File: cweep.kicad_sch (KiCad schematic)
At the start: 59 parts

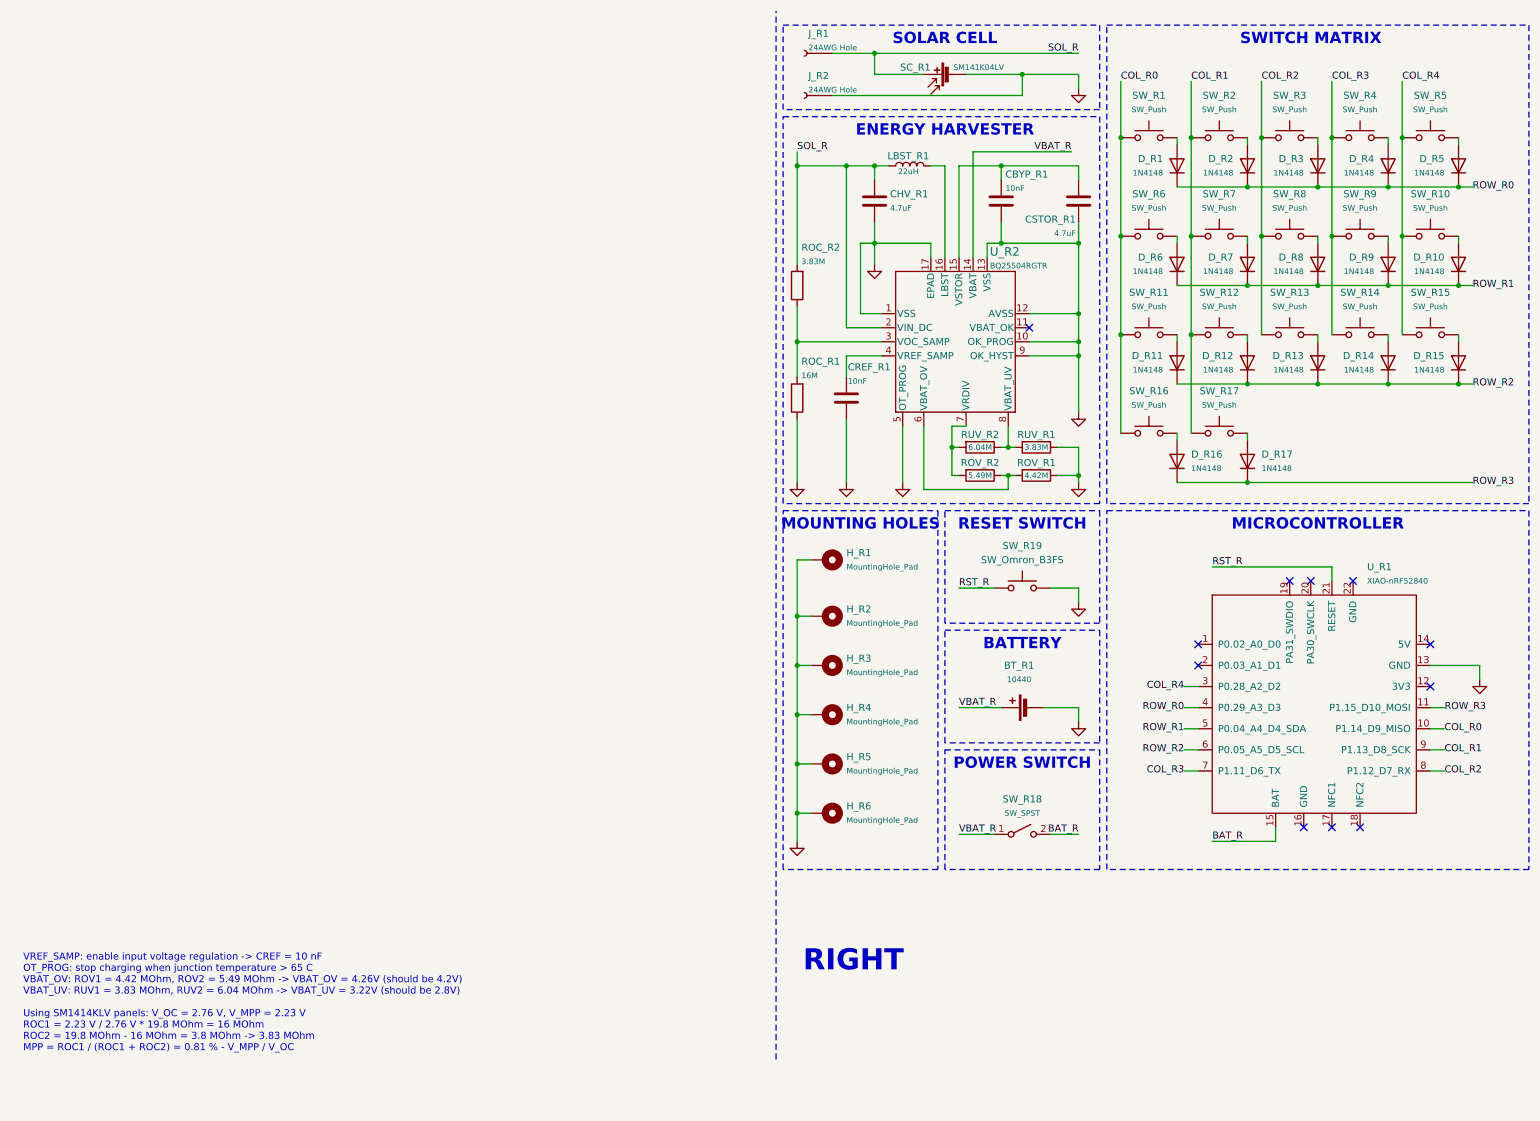
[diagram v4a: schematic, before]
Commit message: feat: add left side of schematic
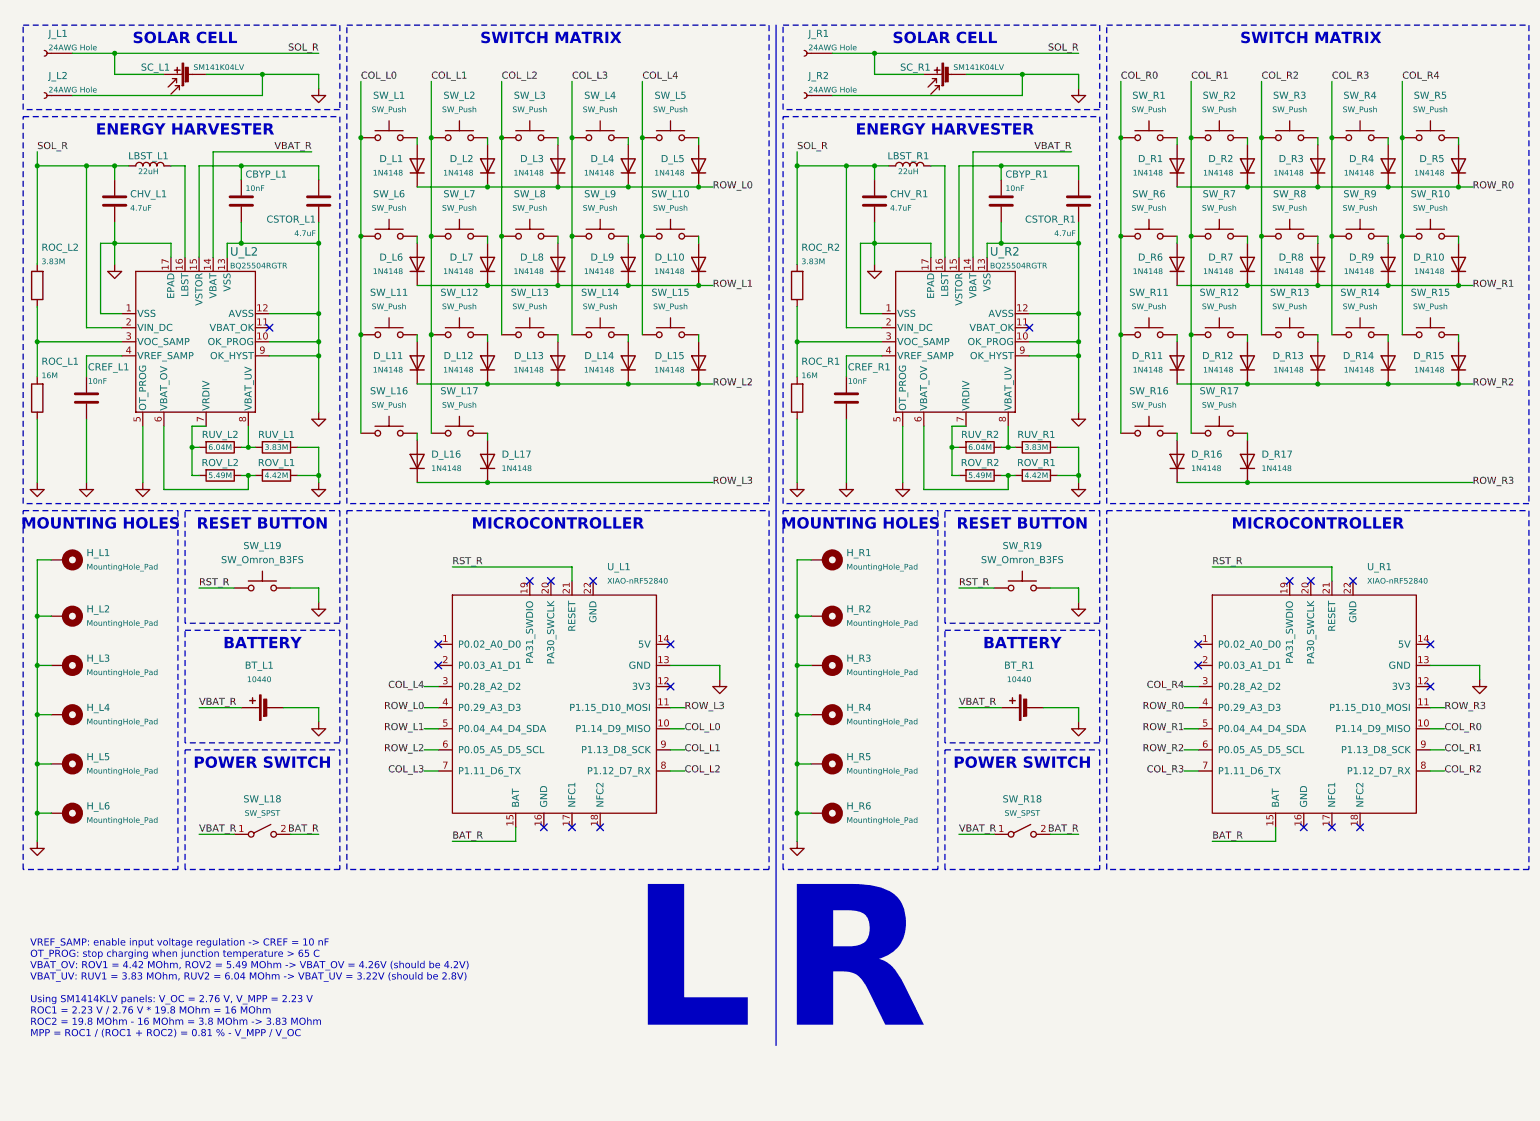
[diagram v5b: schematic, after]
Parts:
- added BT_L1: 10440, com_snapeda_Keystone:BatteryHolder_Keystone_230-1_1x10440, symbol Device:Battery_Cell
- added CBYP_R1, CREF_R1: 10nF, Capacitor_SMD:C_0603_1608Metric_Pad1.08x0.95mm_HandSolder, symbol Device:C
- added CHV_R1, CSTOR_R1: 4.7uF, Capacitor_SMD:C_0603_1608Metric_Pad1.08x0.95mm_HandSolder, symbol Device:C
- added D_R1, D_R10, D_R11, D_R12, D_R13, D_R14, D_R15, D_R16, D_R17, D_R2, D_R3, D_R4, D_R5, D_R6, D_R7, D_R8, D_R9: 1N4148, Diode_THT:D_DO-35_SOD27_P7.62mm_Horizontal, symbol Diode:1N4148
- added H_L1, H_L2, H_L3, H_L4, H_L5, H_L6: MountingHole_Pad, MountingHole:MountingHole_2.2mm_M2_DIN965_Pad_TopOnly, symbol Mechanical:MountingHole_Pad
- added J_R1, J_R2: 24AWG Hole, Connector_Wire:SolderWire-0.127sqmm_1x01_D0.48mm_OD1mm_Relief, symbol Connector:Conn_01x01_Socket
- added LBST_R1: 22uH, Inductor_SMD:L_1210_3225Metric_Pad1.42x2.65mm_HandSolder, symbol Device:L
- added ROC_R1: 16M, Resistor_SMD:R_0603_1608Metric_Pad0.98x0.95mm_HandSolder, symbol Device:R
- added ROC_R2, RUV_R1: 3.83M, Resistor_SMD:R_0603_1608Metric_Pad0.98x0.95mm_HandSolder, symbol Device:R
- added ROV_R1: 4.42M, Resistor_SMD:R_0603_1608Metric_Pad0.98x0.95mm_HandSolder, symbol Device:R
- added ROV_R2: 5.49M, Resistor_SMD:R_0603_1608Metric_Pad0.98x0.95mm_HandSolder, symbol Device:R
- added RUV_R2: 6.04M, Resistor_SMD:R_0603_1608Metric_Pad0.98x0.95mm_HandSolder, symbol Device:R
- added SC_R1: SM141K04LV, cweep:SM141K04LV, symbol Device:Solar_Cell
- added SW_L18: SW_SPST, KAN-15:SW_KAN-15_PHT, symbol Switch:SW_SPST
- added SW_L19: SW_Omron_B3FS, Button_Switch_THT:SW_TH_Tactile_Omron_B3F-10xx, symbol Switch:SW_Omron_B3FS
- added SW_R1, SW_R10, SW_R11, SW_R12, SW_R13, SW_R14, SW_R15, SW_R16, SW_R17, SW_R2, SW_R3, SW_R4, SW_R5, SW_R6, SW_R7, SW_R8, SW_R9: SW_Push, Switch_Keyboard_Hotswap_Kailh:SW_Hotswap_Kailh_Choc_V1_1.00u, symbol Switch:SW_Push
- added U_L1: XIAO-nRF52840, Seeed Studio XIAO Series Library:XIAO-nRF52840, symbol Seeed Studio XIAO Series:XIAO-nRF52840
- added U_R2: BQ25504RGTR, BQ25504RGTR:RGT16_1P7X1P7, symbol BQ25504RGTR:BQ25504RGTR
- renumbered CBYP_R1 to CBYP_L1, CHV_R1 to CHV_L1, CREF_R1 to CREF_L1, CSTOR_R1 to CSTOR_L1, D_R1 to D_L1, D_R10 to D_L10, D_R11 to D_L11, D_R12 to D_L12, D_R13 to D_L13, D_R14 to D_L14, D_R15 to D_L15, D_R16 to D_L16, D_R17 to D_L17, D_R2 to D_L2, D_R3 to D_L3, D_R4 to D_L4, D_R5 to D_L5, D_R6 to D_L6, D_R7 to D_L7, D_R8 to D_L8, D_R9 to D_L9, J_R1 to J_L1, J_R2 to J_L2, LBST_R1 to LBST_L1, ROC_R1 to ROC_L1, ROC_R2 to ROC_L2, ROV_R1 to ROV_L1, ROV_R2 to ROV_L2, RUV_R1 to RUV_L1, RUV_R2 to RUV_L2, SC_R1 to SC_L1, SW_R1 to SW_L1, SW_R10 to SW_L10, SW_R11 to SW_L11, SW_R12 to SW_L12, SW_R13 to SW_L13, SW_R14 to SW_L14, SW_R15 to SW_L15, SW_R16 to SW_L16, SW_R17 to SW_L17, SW_R2 to SW_L2, SW_R3 to SW_L3, SW_R4 to SW_L4, SW_R5 to SW_L5, SW_R6 to SW_L6, SW_R7 to SW_L7, SW_R8 to SW_L8, SW_R9 to SW_L9, U_R2 to U_L2
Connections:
- net BAT_R: now also SW_L18.2 (B), U_L1.15 (BAT)
- net COL_R0: now also SW_R1.1, SW_R11.1, SW_R16.1, SW_R6.1; no longer SW_L1.1, SW_L11.1, SW_L16.1, SW_L6.1
- net COL_R1: now also SW_R12.1, SW_R17.1, SW_R2.1, SW_R7.1; no longer SW_L12.1, SW_L17.1, SW_L2.1, SW_L7.1
- net COL_R2: now also SW_R13.1, SW_R3.1, SW_R8.1; no longer SW_L13.1, SW_L3.1, SW_L8.1
- net COL_R3: now also SW_R14.1, SW_R4.1, SW_R9.1; no longer SW_L14.1, SW_L4.1, SW_L9.1
- net COL_R4: now also SW_R10.1, SW_R15.1, SW_R5.1; no longer SW_L10.1, SW_L15.1, SW_L5.1
- net GND: now also BT_L1.2 (-), CBYP_R1.2, CHV_R1.2, CREF_R1.2, CSTOR_R1.2, H_L1.1, H_L2.1, H_L3.1, H_L4.1, H_L5.1, H_L6.1, J_R2.1 (Pin_1), ROC_R1.1, ROV_R1.1, RUV_R1.1, SC_R1.2 (-), SW_L19.2, U_L1.13 (GND), U_R2.1 (VSS), U_R2.10 (OK_PROG), U_R2.12 (AVSS), U_R2.13 (VSS), U_R2.17 (EPAD), U_R2.5 (OT_PROG), U_R2.9 (OK_HYST)
- net ROW_R0: now also D_R1.1 (K), D_R2.1 (K), D_R3.1 (K), D_R4.1 (K), D_R5.1 (K); no longer D_L1.1 (K), D_L2.1 (K), D_L3.1 (K), D_L4.1 (K), D_L5.1 (K)
- net ROW_R1: now also D_R10.1 (K), D_R6.1 (K), D_R7.1 (K), D_R8.1 (K), D_R9.1 (K); no longer D_L10.1 (K), D_L6.1 (K), D_L7.1 (K), D_L8.1 (K), D_L9.1 (K)
- net ROW_R2: now also D_R11.1 (K), D_R12.1 (K), D_R13.1 (K), D_R14.1 (K), D_R15.1 (K); no longer D_L11.1 (K), D_L12.1 (K), D_L13.1 (K), D_L14.1 (K), D_L15.1 (K)
- net ROW_R3: now also D_R16.1 (K), D_R17.1 (K); no longer D_L16.1 (K), D_L17.1 (K)
- net RST_R: now also SW_L19.1, U_L1.21 (RESET)
- net SOL_R: now also CHV_R1.1, J_R1.1 (Pin_1), LBST_R1.1, ROC_R2.2, SC_R1.1 (+), U_R2.2 (VIN_DC)
- net VBAT_R: now also BT_L1.1 (+), SW_L18.1 (A), U_R2.14 (VBAT)
- new net: D_R3.2 (A), SW_R3.2
- new net: D_R5.2 (A), SW_R5.2
- new net: D_R4.2 (A), SW_R4.2
- new net: D_R2.2 (A), SW_R2.2
- new net: D_R13.2 (A), SW_R13.2
- new net: D_R15.2 (A), SW_R15.2
- new net: ROC_R1.2, ROC_R2.1, U_R2.3 (VOC_SAMP)
- new net: D_R12.2 (A), SW_R12.2
- new net: D_R10.2 (A), SW_R10.2
- new net: D_R8.2 (A), SW_R8.2
- new net: RUV_R1.2, RUV_R2.1, U_R2.8 (VBAT_UV)
- new net: D_R9.2 (A), SW_R9.2
- new net: D_R11.2 (A), SW_R11.2
- new net: ROV_R1.2, ROV_R2.1, U_R2.6 (VBAT_OV)
- new net: D_R6.2 (A), SW_R6.2
- new net: D_R17.2 (A), SW_R17.2
- new net: D_R14.2 (A), SW_R14.2
- new net: CBYP_R1.1, CSTOR_R1.1, U_R2.15 (VSTOR)
- new net: ROV_R2.2, RUV_R2.2, U_R2.7 (VRDIV)
- new net: LBST_R1.2, U_R2.16 (LBST)
- new net: D_R7.2 (A), SW_R7.2
- new net: CREF_R1.1, U_R2.4 (VREF_SAMP)
- new net: D_R16.2 (A), SW_R16.2
- new net: D_R1.2 (A), SW_R1.2
- new net COL_L0: SW_L1.1, SW_L11.1, SW_L16.1, SW_L6.1, U_L1.10 (P1.14_D9_MISO)
- new net COL_L1: SW_L12.1, SW_L17.1, SW_L2.1, SW_L7.1, U_L1.9 (P1.13_D8_SCK)
- new net COL_L2: SW_L13.1, SW_L3.1, SW_L8.1, U_L1.8 (P1.12_D7_RX)
- new net COL_L3: SW_L14.1, SW_L4.1, SW_L9.1, U_L1.7 (P1.11_D6_TX)
- new net COL_L4: SW_L10.1, SW_L15.1, SW_L5.1, U_L1.3 (P0.28_A2_D2)
- new net ROW_L0: D_L1.1 (K), D_L2.1 (K), D_L3.1 (K), D_L4.1 (K), D_L5.1 (K), U_L1.4 (P0.29_A3_D3)
- new net ROW_L1: D_L10.1 (K), D_L6.1 (K), D_L7.1 (K), D_L8.1 (K), D_L9.1 (K), U_L1.5 (P0.04_A4_D4_SDA)
- new net ROW_L2: D_L11.1 (K), D_L12.1 (K), D_L13.1 (K), D_L14.1 (K), D_L15.1 (K), U_L1.6 (P0.05_A5_D5_SCL)
- new net ROW_L3: D_L16.1 (K), D_L17.1 (K), U_L1.11 (P1.15_D10_MOSI)
- no-connect marks 11 -> 22
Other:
- note added: "L"
- note added: "R"
- note added: "RESET BUTTON"
- note removed: "RESET SWITCH"
- note removed: "RIGHT"
- moved on the sheet: CBYP_L1, CHV_L1, CREF_L1, CSTOR_L1, D_L1, D_L10, D_L11, D_L12, D_L13, D_L14, D_L15, D_L16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

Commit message: feat: make keyboard switch reversible
* fix: use SMD diode to accommodate reversible switch
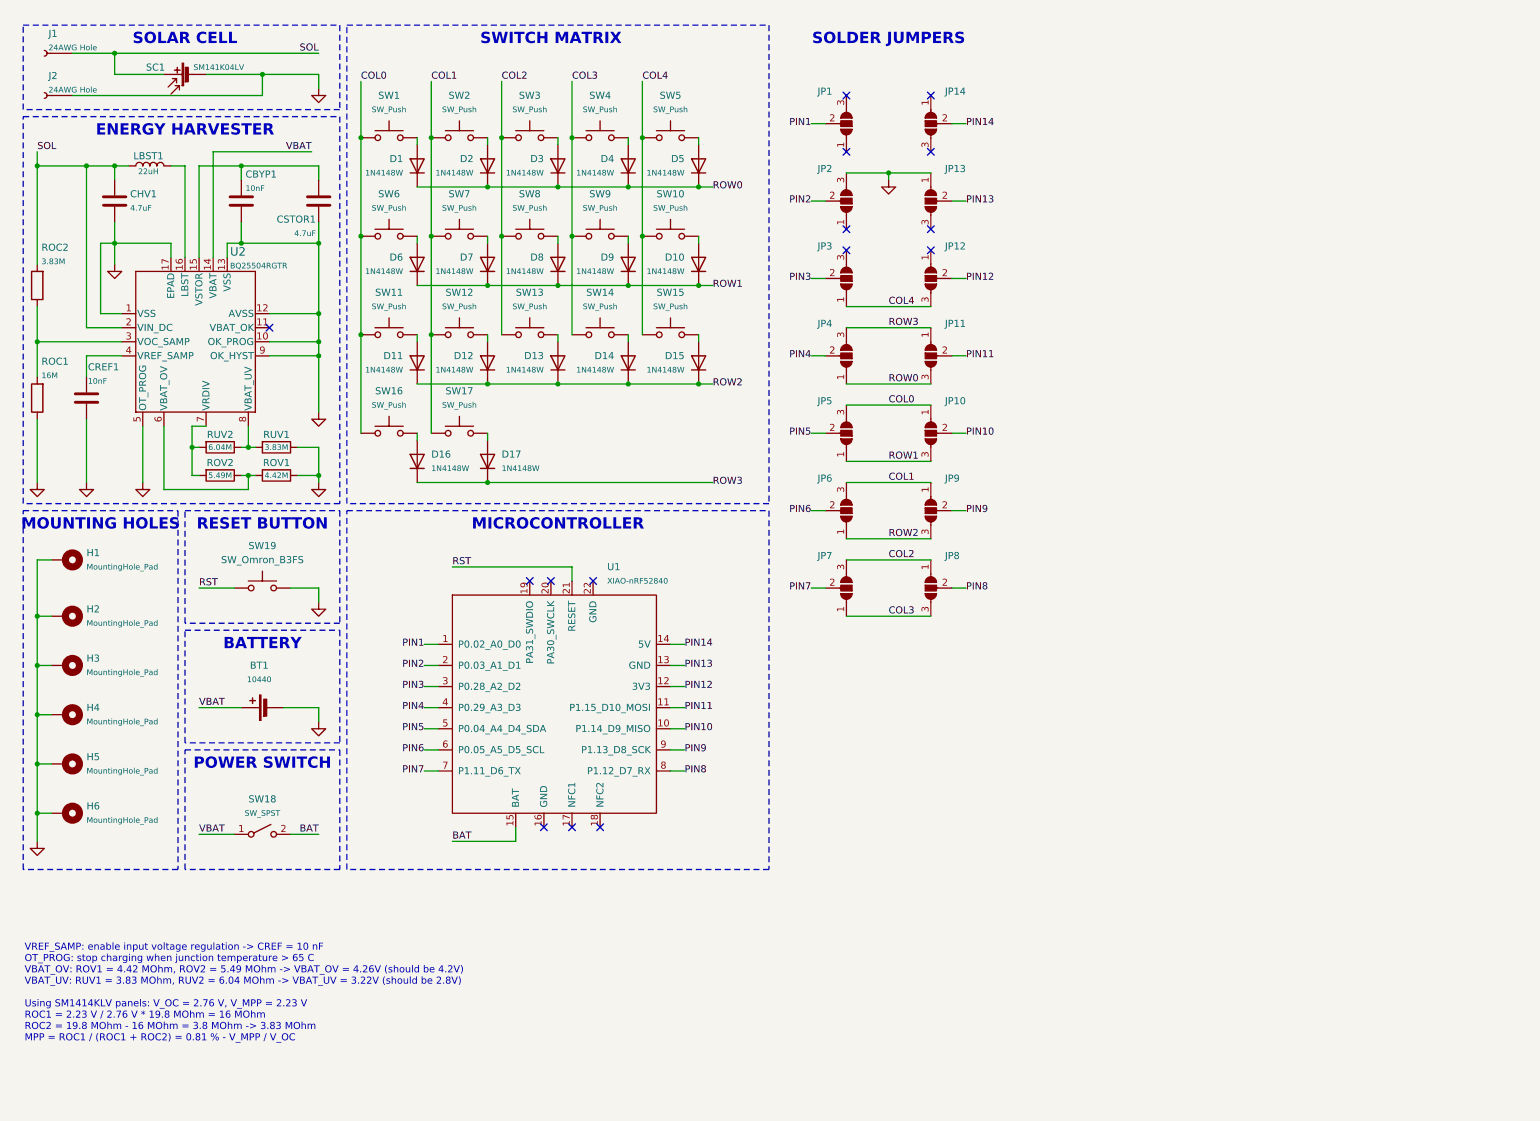
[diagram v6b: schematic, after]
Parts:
- removed BT_L1: 10440, com_snapeda_Keystone:BatteryHolder_Keystone_230-1_1x10440, symbol Device:Battery_Cell
- removed CBYP_L1, CREF_L1: 10nF, Capacitor_SMD:C_0603_1608Metric_Pad1.08x0.95mm_HandSolder, symbol Device:C
- removed CHV_L1, CSTOR_L1: 4.7uF, Capacitor_SMD:C_0603_1608Metric_Pad1.08x0.95mm_HandSolder, symbol Device:C
- removed D_L1, D_L10, D_L11, D_L12, D_L13, D_L14, D_L15, D_L16, D_L17, D_L2, D_L3, D_L4, D_L5, D_L6, D_L7, D_L8, D_L9: 1N4148, Diode_THT:D_DO-35_SOD27_P7.62mm_Horizontal, symbol Diode:1N4148
- removed H_L1, H_L2, H_L3, H_L4, H_L5, H_L6: MountingHole_Pad, MountingHole:MountingHole_2.2mm_M2_DIN965_Pad_TopOnly, symbol Mechanical:MountingHole_Pad
- removed J_L1, J_L2: 24AWG Hole, Connector_Wire:SolderWire-0.127sqmm_1x01_D0.48mm_OD1mm_Relief, symbol Connector:Conn_01x01_Socket
- removed LBST_L1: 22uH, Inductor_SMD:L_1210_3225Metric_Pad1.42x2.65mm_HandSolder, symbol Device:L
- removed ROC_L1: 16M, Resistor_SMD:R_0603_1608Metric_Pad0.98x0.95mm_HandSolder, symbol Device:R
- removed ROC_L2, RUV_L1: 3.83M, Resistor_SMD:R_0603_1608Metric_Pad0.98x0.95mm_HandSolder, symbol Device:R
- removed ROV_L1: 4.42M, Resistor_SMD:R_0603_1608Metric_Pad0.98x0.95mm_HandSolder, symbol Device:R
- removed ROV_L2: 5.49M, Resistor_SMD:R_0603_1608Metric_Pad0.98x0.95mm_HandSolder, symbol Device:R
- removed RUV_L2: 6.04M, Resistor_SMD:R_0603_1608Metric_Pad0.98x0.95mm_HandSolder, symbol Device:R
- removed SC_L1: SM141K04LV, cweep:SM141K04LV, symbol Device:Solar_Cell
- removed SW_L1, SW_L10, SW_L11, SW_L12, SW_L13, SW_L14, SW_L15, SW_L16, SW_L17, SW_L2, SW_L3, SW_L4, SW_L5, SW_L6, SW_L7, SW_L8, SW_L9: SW_Push, Switch_Keyboard_Hotswap_Kailh:SW_Hotswap_Kailh_Choc_V1_1.00u, symbol Switch:SW_Push
- removed SW_L18: SW_SPST, KAN-15:SW_KAN-15_PHT, symbol Switch:SW_SPST
- removed SW_L19: SW_Omron_B3FS, Button_Switch_THT:SW_TH_Tactile_Omron_B3F-10xx, symbol Switch:SW_Omron_B3FS
- removed U_L1: XIAO-nRF52840, Seeed Studio XIAO Series Library:XIAO-nRF52840, symbol Seeed Studio XIAO Series:XIAO-nRF52840
- removed U_L2: BQ25504RGTR, BQ25504RGTR:RGT16_1P7X1P7, symbol BQ25504RGTR:BQ25504RGTR
- added JP1, JP10, JP11, JP12, JP13, JP14, JP2, JP3, JP4, JP5, JP6, JP7, JP8, JP9: SolderJumper_3_Open, cweep:SolderJumper-3_P2.0mm_Open_TrianglePad1.0x1.5mm_Reversible, symbol Jumper:SolderJumper_3_Open
- D1: renamed from D_R1; value 1N4148 -> 1N4148W; footprint Diode_THT:D_DO-35_SOD27_P7.62mm_Horizontal -> cweep:D_SOD-123_Reversible; symbol Diode:1N4148 -> Diode:1N4148W
- D10: renamed from D_R10; value 1N4148 -> 1N4148W; footprint Diode_THT:D_DO-35_SOD27_P7.62mm_Horizontal -> cweep:D_SOD-123_Reversible; symbol Diode:1N4148 -> Diode:1N4148W
- D11: renamed from D_R11; value 1N4148 -> 1N4148W; footprint Diode_THT:D_DO-35_SOD27_P7.62mm_Horizontal -> cweep:D_SOD-123_Reversible; symbol Diode:1N4148 -> Diode:1N4148W
- D12: renamed from D_R12; value 1N4148 -> 1N4148W; footprint Diode_THT:D_DO-35_SOD27_P7.62mm_Horizontal -> cweep:D_SOD-123_Reversible; symbol Diode:1N4148 -> Diode:1N4148W
- D13: renamed from D_R13; value 1N4148 -> 1N4148W; footprint Diode_THT:D_DO-35_SOD27_P7.62mm_Horizontal -> cweep:D_SOD-123_Reversible; symbol Diode:1N4148 -> Diode:1N4148W
- D14: renamed from D_R14; value 1N4148 -> 1N4148W; footprint Diode_THT:D_DO-35_SOD27_P7.62mm_Horizontal -> cweep:D_SOD-123_Reversible; symbol Diode:1N4148 -> Diode:1N4148W
- D15: renamed from D_R15; value 1N4148 -> 1N4148W; footprint Diode_THT:D_DO-35_SOD27_P7.62mm_Horizontal -> cweep:D_SOD-123_Reversible; symbol Diode:1N4148 -> Diode:1N4148W
- D16: renamed from D_R16; value 1N4148 -> 1N4148W; footprint Diode_THT:D_DO-35_SOD27_P7.62mm_Horizontal -> cweep:D_SOD-123_Reversible; symbol Diode:1N4148 -> Diode:1N4148W
- D17: renamed from D_R17; value 1N4148 -> 1N4148W; footprint Diode_THT:D_DO-35_SOD27_P7.62mm_Horizontal -> cweep:D_SOD-123_Reversible; symbol Diode:1N4148 -> Diode:1N4148W
- D2: renamed from D_R2; value 1N4148 -> 1N4148W; footprint Diode_THT:D_DO-35_SOD27_P7.62mm_Horizontal -> cweep:D_SOD-123_Reversible; symbol Diode:1N4148 -> Diode:1N4148W
- D3: renamed from D_R3; value 1N4148 -> 1N4148W; footprint Diode_THT:D_DO-35_SOD27_P7.62mm_Horizontal -> cweep:D_SOD-123_Reversible; symbol Diode:1N4148 -> Diode:1N4148W
- D4: renamed from D_R4; value 1N4148 -> 1N4148W; footprint Diode_THT:D_DO-35_SOD27_P7.62mm_Horizontal -> cweep:D_SOD-123_Reversible; symbol Diode:1N4148 -> Diode:1N4148W
- D5: renamed from D_R5; value 1N4148 -> 1N4148W; footprint Diode_THT:D_DO-35_SOD27_P7.62mm_Horizontal -> cweep:D_SOD-123_Reversible; symbol Diode:1N4148 -> Diode:1N4148W
- D6: renamed from D_R6; value 1N4148 -> 1N4148W; footprint Diode_THT:D_DO-35_SOD27_P7.62mm_Horizontal -> cweep:D_SOD-123_Reversible; symbol Diode:1N4148 -> Diode:1N4148W
- D7: renamed from D_R7; value 1N4148 -> 1N4148W; footprint Diode_THT:D_DO-35_SOD27_P7.62mm_Horizontal -> cweep:D_SOD-123_Reversible; symbol Diode:1N4148 -> Diode:1N4148W
- D8: renamed from D_R8; value 1N4148 -> 1N4148W; footprint Diode_THT:D_DO-35_SOD27_P7.62mm_Horizontal -> cweep:D_SOD-123_Reversible; symbol Diode:1N4148 -> Diode:1N4148W
- D9: renamed from D_R9; value 1N4148 -> 1N4148W; footprint Diode_THT:D_DO-35_SOD27_P7.62mm_Horizontal -> cweep:D_SOD-123_Reversible; symbol Diode:1N4148 -> Diode:1N4148W
- SW1: renamed from SW_R1; footprint Switch_Keyboard_Hotswap_Kailh:SW_Hotswap_Kailh_Choc_V1_1.00u -> cweep:SW_Hotswap_Kailh_Choc_V1_1.00u_Reversible
- SW10: renamed from SW_R10; footprint Switch_Keyboard_Hotswap_Kailh:SW_Hotswap_Kailh_Choc_V1_1.00u -> cweep:SW_Hotswap_Kailh_Choc_V1_1.00u_Reversible
- SW11: renamed from SW_R11; footprint Switch_Keyboard_Hotswap_Kailh:SW_Hotswap_Kailh_Choc_V1_1.00u -> cweep:SW_Hotswap_Kailh_Choc_V1_1.00u_Reversible
- SW12: renamed from SW_R12; footprint Switch_Keyboard_Hotswap_Kailh:SW_Hotswap_Kailh_Choc_V1_1.00u -> cweep:SW_Hotswap_Kailh_Choc_V1_1.00u_Reversible
- SW13: renamed from SW_R13; footprint Switch_Keyboard_Hotswap_Kailh:SW_Hotswap_Kailh_Choc_V1_1.00u -> cweep:SW_Hotswap_Kailh_Choc_V1_1.00u_Reversible
- SW14: renamed from SW_R14; footprint Switch_Keyboard_Hotswap_Kailh:SW_Hotswap_Kailh_Choc_V1_1.00u -> cweep:SW_Hotswap_Kailh_Choc_V1_1.00u_Reversible
- SW15: renamed from SW_R15; footprint Switch_Keyboard_Hotswap_Kailh:SW_Hotswap_Kailh_Choc_V1_1.00u -> cweep:SW_Hotswap_Kailh_Choc_V1_1.00u_Reversible
- SW16: renamed from SW_R16; footprint Switch_Keyboard_Hotswap_Kailh:SW_Hotswap_Kailh_Choc_V1_1.00u -> cweep:SW_Hotswap_Kailh_Choc_V1_1.00u_Reversible
- SW17: renamed from SW_R17; footprint Switch_Keyboard_Hotswap_Kailh:SW_Hotswap_Kailh_Choc_V1_1.00u -> cweep:SW_Hotswap_Kailh_Choc_V1_1.00u_Reversible
- SW2: renamed from SW_R2; footprint Switch_Keyboard_Hotswap_Kailh:SW_Hotswap_Kailh_Choc_V1_1.00u -> cweep:SW_Hotswap_Kailh_Choc_V1_1.00u_Reversible
- SW3: renamed from SW_R3; footprint Switch_Keyboard_Hotswap_Kailh:SW_Hotswap_Kailh_Choc_V1_1.00u -> cweep:SW_Hotswap_Kailh_Choc_V1_1.00u_Reversible
- SW4: renamed from SW_R4; footprint Switch_Keyboard_Hotswap_Kailh:SW_Hotswap_Kailh_Choc_V1_1.00u -> cweep:SW_Hotswap_Kailh_Choc_V1_1.00u_Reversible
- SW5: renamed from SW_R5; footprint Switch_Keyboard_Hotswap_Kailh:SW_Hotswap_Kailh_Choc_V1_1.00u -> cweep:SW_Hotswap_Kailh_Choc_V1_1.00u_Reversible
- SW6: renamed from SW_R6; footprint Switch_Keyboard_Hotswap_Kailh:SW_Hotswap_Kailh_Choc_V1_1.00u -> cweep:SW_Hotswap_Kailh_Choc_V1_1.00u_Reversible
- SW7: renamed from SW_R7; footprint Switch_Keyboard_Hotswap_Kailh:SW_Hotswap_Kailh_Choc_V1_1.00u -> cweep:SW_Hotswap_Kailh_Choc_V1_1.00u_Reversible
- SW8: renamed from SW_R8; footprint Switch_Keyboard_Hotswap_Kailh:SW_Hotswap_Kailh_Choc_V1_1.00u -> cweep:SW_Hotswap_Kailh_Choc_V1_1.00u_Reversible
- SW9: renamed from SW_R9; footprint Switch_Keyboard_Hotswap_Kailh:SW_Hotswap_Kailh_Choc_V1_1.00u -> cweep:SW_Hotswap_Kailh_Choc_V1_1.00u_Reversible
- renumbered BT_R1 to BT1, CBYP_R1 to CBYP1, CHV_R1 to CHV1, CREF_R1 to CREF1, CSTOR_R1 to CSTOR1, H_R1 to H1, H_R2 to H2, H_R3 to H3, H_R4 to H4, H_R5 to H5, H_R6 to H6, J_R1 to J1, J_R2 to J2, LBST_R1 to LBST1, ROC_R1 to ROC1, ROC_R2 to ROC2, ROV_R1 to ROV1, ROV_R2 to ROV2, RUV_R1 to RUV1, RUV_R2 to RUV2, SC_R1 to SC1, SW_R18 to SW18, SW_R19 to SW19, U_R1 to U1, U_R2 to U2
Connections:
- net GND: now also JP13.1 (A), JP2.3 (B); no longer U1.13 (GND)
- net PIN1: now reaches U1.1 (P0.02_A0_D0)
- net PIN1: now also JP1.2 (C)
- net PIN12: now reaches U1.12 (3V3)
- net PIN12: now also JP12.2 (C)
- net PIN14: now reaches U1.14 (5V)
- net PIN14: now also JP14.2 (C)
- net PIN2: now reaches U1.2 (P0.03_A1_D1)
- net PIN2: now also JP2.2 (C)
- net BAT_R renamed BAT
- net COL_R0 renamed COL0
- net COL0: now also JP10.1 (A), JP5.3 (B); no longer U1.10 (P1.14_D9_MISO)
- net COL_R1 renamed COL1
- net COL1: now also JP6.3 (B), JP9.1 (A); no longer U1.9 (P1.13_D8_SCK)
- net COL_R2 renamed COL2
- net COL2: now also JP7.3 (B), JP8.1 (A); no longer U1.8 (P1.12_D7_RX)
- net COL_R3 renamed COL3
- net COL3: now also JP7.1 (A), JP8.3 (B); no longer U1.7 (P1.11_D6_TX)
- net COL_R4 renamed COL4
- net COL4: now also JP12.3 (B), JP3.1 (A); no longer U1.3 (P0.28_A2_D2)
- net ROW_R0 renamed ROW0
- net ROW0: now also JP11.3 (B), JP4.1 (A); no longer U1.4 (P0.29_A3_D3)
- net ROW_R1 renamed ROW1
- net ROW1: now also JP10.3 (B), JP5.1 (A); no longer U1.5 (P0.04_A4_D4_SDA)
- net ROW_R2 renamed ROW2
- net ROW2: now also JP6.1 (A), JP9.3 (B); no longer U1.6 (P0.05_A5_D5_SCL)
- net ROW_R3 renamed ROW3
- net ROW3: now also JP11.1 (A), JP4.3 (B); no longer U1.11 (P1.15_D10_MOSI)
- net RST_R renamed RST
- net SOL_R renamed SOL
- net VBAT_R renamed VBAT
- new net PIN10: JP10.2 (C), U1.10 (P1.14_D9_MISO)
- new net PIN11: JP11.2 (C), U1.11 (P1.15_D10_MOSI)
- new net PIN13: JP13.2 (C), U1.13 (GND)
- new net PIN3: JP3.2 (C), U1.3 (P0.28_A2_D2)
- new net PIN4: JP4.2 (C), U1.4 (P0.29_A3_D3)
- new net PIN5: JP5.2 (C), U1.5 (P0.04_A4_D4_SDA)
- new net PIN6: JP6.2 (C), U1.6 (P0.05_A5_D5_SCL)
- new net PIN7: JP7.2 (C), U1.7 (P1.11_D6_TX)
- new net PIN8: JP8.2 (C), U1.8 (P1.12_D7_RX)
- new net PIN9: JP9.2 (C), U1.9 (P1.13_D8_SCK)
- no-connect marks 22 -> 15
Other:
- note added: "SOLDER JUMPERS"
- note removed: "L"
- note removed: "R"
- moved on the sheet: BT1, CBYP1, CHV1, CREF1, CSTOR1, D1, D10, D11, D12, D13, D14, D15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
